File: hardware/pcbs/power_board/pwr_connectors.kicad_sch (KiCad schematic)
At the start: 3 parts, among them J14 ScrewTerminal_02, J15 MTA100_02, J16 MTA100_02

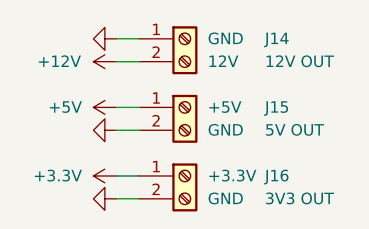
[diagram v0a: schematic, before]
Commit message: power_board: THERE ARE FOUR FANS
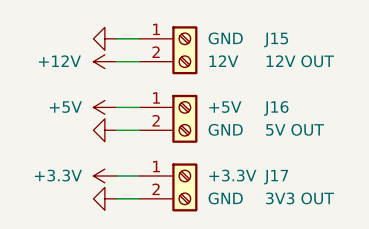
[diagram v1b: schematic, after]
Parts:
- renumbered J14 to J15, J15 to J16, J16 to J17
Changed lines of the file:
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@@
 		(dnp no)
 		(fields_autoplaced yes)
-		(property "Reference" "#PWR0103"
+		(property "Reference" "#PWR0109"
 			(at 139.7 104.14 0)
 			(effects
@@
 			(project "power_board"
 				(path "/4b166175-80a4-48c6-994d-6e62a6160b87/eb6931d2-84dc-4c44-a536-817b4a1688b3"
-					(reference "#PWR0103")
+					(reference "#PWR0109")
 					(unit 1)
 				)
@@
 		(dnp no)
 		(fields_autoplaced yes)
-		(property "Reference" "#PWR099"
+		(property "Reference" "#PWR0105"
 			(at 129.54 88.9 0)
 			(effects
@@
 			(project "power_board"
 				(path "/4b166175-80a4-48c6-994d-6e62a6160b87/eb6931d2-84dc-4c44-a536-817b4a1688b3"
-					(reference "#PWR099")
+					(reference "#PWR0105")
 					(unit 1)
 				)
@@
 		(dnp no)
 		(fields_autoplaced yes)
-		(property "Reference" "#PWR0101"
+		(property "Reference" "#PWR0107"
 			(at 139.7 96.52 0)
 			(effects
@@
 			(project "power_board"
 				(path "/4b166175-80a4-48c6-994d-6e62a6160b87/eb6931d2-84dc-4c44-a536-817b4a1688b3"
-					(reference "#PWR0101")
+					(reference "#PWR0107")
 					(unit 1)
 				)
@@
 		(dnp no)
 		(fields_autoplaced yes)
-		(property "Reference" "#PWR0102"
+		(property "Reference" "#PWR0108"
 			(at 129.54 99.06 0)
 			(effects
@@
 			(project "power_board"
 				(path "/4b166175-80a4-48c6-994d-6e62a6160b87/eb6931d2-84dc-4c44-a536-817b4a1688b3"
-					(reference "#PWR0102")
+					(reference "#PWR0108")
 					(unit 1)
 				)
@@
 		(dnp no)
 		(fields_autoplaced yes)
-		(property "Reference" "#PWR0104"
+		(property "Reference" "#PWR0110"
 			(at 129.54 106.68 0)
 			(effects
@@
 			(project "power_board"
 				(path "/4b166175-80a4-48c6-994d-6e62a6160b87/eb6931d2-84dc-4c44-a536-817b4a1688b3"
-					(reference "#PWR0104")
+					(reference "#PWR0110")
 					(unit 1)
 				)
@@
 		(on_board yes)
 		(dnp no)
-		(property "Reference" "J14"
+		(property "Reference" "J15"
 			(at 152.4 88.9 0)
 			(effects
@@
 			(project "power_board"
 				(path "/4b166175-80a4-48c6-994d-6e62a6160b87/eb6931d2-84dc-4c44-a536-817b4a1688b3"
-					(reference "J14")
+					(reference "J15")
 					(unit 1)
 				)
@@
 		(on_board yes)
 		(dnp no)
-		(property "Reference" "#PWR0100"
+		(property "Reference" "#PWR0106"
 			(at 139.7 91.44 0)
 			(effects
@@
 			(project "power_board"
 				(path "/4b166175-80a4-48c6-994d-6e62a6160b87/eb6931d2-84dc-4c44-a536-817b4a1688b3"
-					(reference "#PWR0100")
+					(reference "#PWR0106")
 					(unit 1)
 				)
@@
 		(on_board yes)
 		(dnp no)
-		(property "Reference" "J16"
+		(property "Reference" "J17"
 			(at 152.4 104.14 0)
 			(effects
@@
 			(project "power_board"
 				(path "/4b166175-80a4-48c6-994d-6e62a6160b87/eb6931d2-84dc-4c44-a536-817b4a1688b3"
-					(reference "J16")
+					(reference "J17")
 					(unit 1)
 				)
@@
 		(on_board yes)
 		(dnp no)
-		(property "Reference" "J15"
+		(property "Reference" "J16"
 			(at 152.4 96.52 0)
 			(effects
@@
 			(project "power_board"
 				(path "/4b166175-80a4-48c6-994d-6e62a6160b87/eb6931d2-84dc-4c44-a536-817b4a1688b3"
-					(reference "J15")
-					(unit 1)
-				)
+					(reference "J16")
+					(unit 1)
+				)
